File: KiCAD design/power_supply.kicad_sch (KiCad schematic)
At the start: 7 parts, among them U301 A71117CH2-5.0TRG1, U302 MIC5317

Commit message: Fixes
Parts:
- C301: value 10uF -> 1uF; Price 0.29 -> 0.13; PurchaseLoc https://www.digikey.fi/fi/products/detail/yageo/CC0805KKX5R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 -> https://www.digikey.fi/fi/products/detail/yageo/CC0805KKX7R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
- C302: value 22uF -> 1uF; Price 0.09 -> 0.13; PurchaseLoc https://www.digikey.fi/fi/products/detail/yageo/CC0805JRNPO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 -> https://www.digikey.fi/fi/products/detail/yageo/CC0805KKX7R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
- U301: value A71117CH2-5.0TRG1 -> MCP1804T
- U302: PurchaseLoc https://www.digikey.fi/en/products/detail/microchip-technol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 -> https://www.digikey.fi/fi/products/detail/microchip-technol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
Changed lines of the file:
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@@
       (effects (font (size 1.27 1.27)) (justify left))
     )
-    (property "Value" "10uF" (id 1) (at 45.72 62.2362 0)
+    (property "Value" "1uF" (id 1) (at 45.72 62.2362 0)
       (effects (font (size 1.27 1.27)) (justify left))
     )
@@
       (effects (font (size 1.27 1.27)) hide)
     )
-    (property "Datasheet" "https://www.yageo.com/upload/media/product/productsearch/datasheet/mlcc/UPY-GPHC_X5R_4V-to-50V_26.pdf" (id 3) (at 43.18 60.96 0)
+    (property "Datasheet" "https://www.yageo.com/upload/media/product/productsearch/datasheet/mlcc/UPY-GPHC_X7R_6.3V-to-250V_22.pdf" (id 3) (at 43.18 60.96 0)
       (effects (font (size 1.27 1.27)) hide)
     )
-    (property "PurchaseLoc" "https://www.digikey.fi/fi/products/detail/yageo/CC0805KKX5R8BB106/5195275" (id 4) (at 43.18 60.96 0)
+    (property "PurchaseLoc" "https://www.digikey.fi/fi/products/detail/yageo/CC0805KKX7R7BB105/2103103" (id 4) (at 43.18 60.96 0)
       (effects (font (size 1.27 1.27)) hide)
     )
-    (property "Price" "0.29" (id 5) (at 43.18 60.96 0)
+    (property "Price" "0.13" (id 5) (at 43.18 60.96 0)
       (effects (font (size 1.27 1.27)) hide)
     )
@@
       (effects (font (size 1.27 1.27) italic) (justify left) hide)
     )
-    (property "Datasheet" "http://ww1.microchip.com/downloads/en/DeviceDoc/22053C.pdf" (id 3) (at 133.35 59.055 0)
+    (property "Datasheet" "https://ww1.microchip.com/downloads/en/DeviceDoc/MIC5317-High-Performance-Single-150mA-LDO-DS20006195B.pdf" (id 3) (at 133.35 59.055 0)
       (effects (font (size 1.27 1.27)) hide)
     )
-    (property "PurchaseLoc" "https://www.digikey.fi/en/products/detail/microchip-technology/MCP1802T-3302I-OT/1679144" (id 4) (at 133.35 56.515 0)
+    (property "PurchaseLoc" "https://www.digikey.fi/fi/products/detail/microchip-technology/MIC5317-2-8YM5-TR/5049114" (id 4) (at 133.35 56.515 0)
       (effects (font (size 1.27 1.27)) hide)
     )
@@
     (in_bom yes) (on_board yes) (fields_autoplaced)
     (property "Reference" "U301" (id 0) (at 56.134 49.022 0))
-    (property "Value" "A71117CH2-5.0TRG1" (id 1) (at 56.134 51.562 0))
+    (property "Value" "MCP1804T" (id 1) (at 56.134 51.562 0))
     (property "Footprint" "Package_TO_SOT_SMD:SOT-223-3_TabPin2" (id 2) (at 56.134 50.8 0)
       (effects (font (size 1.27 1.27)) hide)
@@
       (effects (font (size 1.27 1.27)) (justify left))
     )
-    (property "Value" "22uF" (id 1) (at 71.12 60.9662 0)
+    (property "Value" "1uF" (id 1) (at 71.12 60.9662 0)
       (effects (font (size 1.27 1.27)) (justify left))
     )
@@
       (effects (font (size 1.27 1.27)) hide)
     )
-    (property "Datasheet" "https://www.yageo.com/upload/media/product/productsearch/datasheet/mlcc/UPY-GP_NP0_16V-to-50V_18.pdf" (id 3) (at 67.818 59.69 0)
+    (property "Datasheet" "https://www.yageo.com/upload/media/product/productsearch/datasheet/mlcc/UPY-GPHC_X7R_6.3V-to-250V_22.pdf" (id 3) (at 67.818 59.69 0)
       (effects (font (size 1.27 1.27)) hide)
     )
-    (property "PurchaseLoc" "https://www.digikey.fi/fi/products/detail/yageo/CC0805JRNPO9BN220/302837" (id 4) (at 67.818 59.69 0)
+    (property "PurchaseLoc" "https://www.digikey.fi/fi/products/detail/yageo/CC0805KKX7R7BB105/2103103" (id 4) (at 67.818 59.69 0)
       (effects (font (size 1.27 1.27)) hide)
     )
-    (property "Price" "0.09" (id 5) (at 67.818 59.69 0)
+    (property "Price" "0.13" (id 5) (at 67.818 59.69 0)
       (effects (font (size 1.27 1.27)) hide)
     )

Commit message: more comments (no changes in functionality)
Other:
- note added: "3.3 V will be used to power the Pmod BLE bluetooth module."
- note added: "5 V voltage will be used to power the TOF sensors, the current sensor, and the Nucleo board."
- note added: "Main power switch."
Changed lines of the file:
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@@
     (stroke (width 0) (type default) (color 0 0 0 0))
+  )
+  (text "Main power switch." (at 182.88 72.39 0)
+    (effects (font (size 1.27 1.27)) (justify left bottom))
   )
   (text "SWITCH" (at 168.275 20.32 0)
@@
     (effects (font (size 3.81 3.81)) (justify left bottom))
   )
+  (text "5 V voltage will be used to power the TOF sensors,\nthe current sensor, and the Nucleo board."
+    (at 16.51 78.74 0)
+    (effects (font (size 1.27 1.27)) (justify left bottom))
+  )
+  (text "3.3 V will be used to power the Pmod BLE bluetooth module."
+    (at 99.06 77.47 0)
+    (effects (font (size 1.27 1.27)) (justify left bottom))
+  )
   (text "Bypass capacitor\nas close to the LDO (pin 1 VIN) as possible\n"

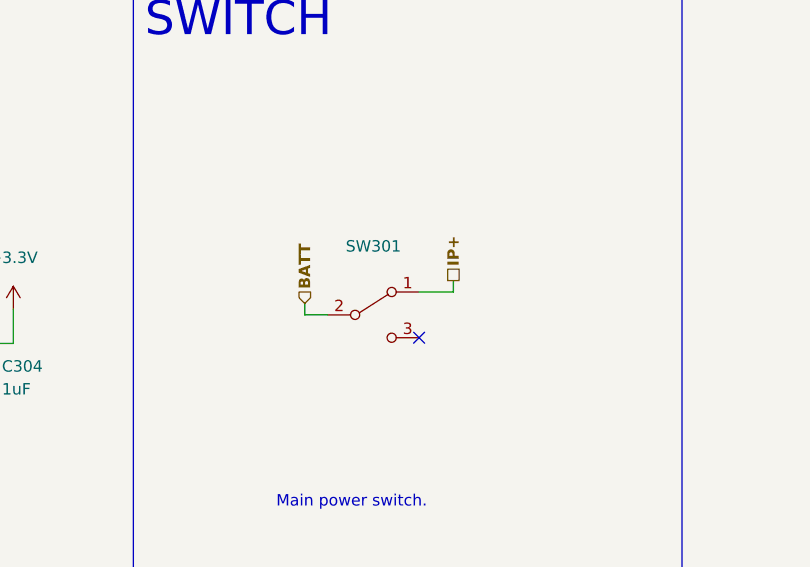
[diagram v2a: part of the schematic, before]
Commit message: change in nucleo pin
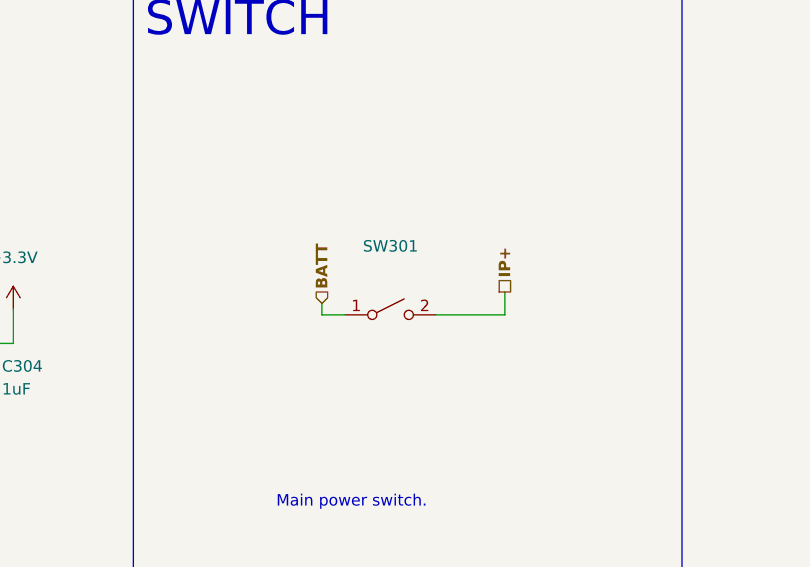
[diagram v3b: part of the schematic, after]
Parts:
- SW301: footprint composants_projet_footprint:1A11-NF5STSE-B -> SWITCH lib:E-SWITCH_RR511D1121; symbol Switch:SW_SPDT -> Switch:SW_SPST
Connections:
- net BATT: now also SW301.1 (A); no longer SW301.2 (B)
- net IP+: now also SW301.2 (B); no longer SW301.1 (A)
- no-connect marks 1 -> 0
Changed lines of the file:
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@@
   (junction (at 120.65 53.975) (diameter 0) (color 0 0 0 0)
   )
-  (no_connect (at 198.755 53.34))
+  (wire (pts (xy 208.28 50.8) (xy 200.66 50.8))
+    (stroke (width 0) (type default) (color 0 0 0 0))
+  )
   (wire (pts (xy 43.18 55.88) (xy 48.514 55.88))
     (stroke (width 0) (type default) (color 0 0 0 0))
@@
     (stroke (width 0) (type default) (color 0 0 0 0))
   )
-  (wire (pts (xy 202.565 48.26) (xy 198.755 48.26))
-    (stroke (width 0) (type default) (color 0 0 0 0))
-  )
   (wire (pts (xy 133.35 65.405) (xy 133.35 66.675))
     (stroke (width 0) (type default) (color 0 0 0 0))
@@
     (stroke (width 0) (type default) (color 0 0 0 0))
   )
-  (wire (pts (xy 188.595 50.8) (xy 186.055 50.8))
+  (wire (pts (xy 190.5 50.8) (xy 187.96 50.8))
     (stroke (width 0) (type default) (color 0 0 0 0))
   )
@@
     (stroke (width 0) (type default) (color 0 0 0 0))
   )
-  (wire (pts (xy 202.565 46.99) (xy 202.565 48.26))
-    (stroke (width 0) (type default) (color 0 0 0 0))
-  )
   (wire (pts (xy 120.65 53.975) (xy 123.19 53.975))
     (stroke (width 0) (type default) (color 0 0 0 0))
@@
     (stroke (width 0) (type default) (color 0 0 0 0))
   )
+  (wire (pts (xy 208.28 48.26) (xy 208.28 50.8))
+    (stroke (width 0) (type default) (color 0 0 0 0))
+  )
   (wire (pts (xy 63.754 55.88) (xy 67.818 55.88))
     (stroke (width 0) (type default) (color 0 0 0 0))
@@
     (stroke (width 0) (type default) (color 0 0 0 0))
   )
-  (wire (pts (xy 186.055 50.8) (xy 186.055 49.53))
+  (wire (pts (xy 187.96 50.8) (xy 187.96 49.53))
     (stroke (width 0) (type default) (color 0 0 0 0))
   )
@@
     (effects (font (size 3.81 3.81)) (justify left bottom))
   )
-  (hierarchical_label "BATT" (shape input) (at 186.055 49.53 90)
+  (hierarchical_label "BATT" (shape input) (at 187.96 49.53 90)
     (effects (font (size 1.27 1.27) bold) (justify left))
   )
-  (hierarchical_label "IP+" (shape passive) (at 202.565 46.99 90)
+  (hierarchical_label "IP+" (shape passive) (at 208.28 48.26 90)
     (effects (font (size 1.27 1.27) bold) (justify left))
   )
@@
     (pin "2")
   )
-  (symbol (lib_id "Switch:SW_SPDT") (at 193.675 50.8 0) (unit 1)
-    (in_bom yes) (on_board yes) (fields_autoplaced)
-    (property "Reference" "SW301" (id 0) (at 193.675 43.18 0))
-    (property "Value" "~" (id 1) (at 193.675 45.72 0))
-    (property "Footprint" "composants_projet_footprint:1A11-NF5STSE-B" (id 2) (at 193.675 50.8 0)
-      (effects (font (size 1.27 1.27)) hide)
-    )
-    (property "Datasheet" "~" (id 3) (at 193.675 50.8 0)
-      (effects (font (size 1.27 1.27)) hide)
-    )
-    (property "Price" "1.05" (id 4) (at 193.675 50.8 0)
-      (effects (font (size 1.27 1.27)) hide)
-    )
-    (property "PurchaseLoc" "https://www.digikey.com/en/products/detail/e-switch/RR511D1121/2116256" (id 5) (at 193.675 50.8 0)
-      (effects (font (size 1.27 1.27)) hide)
-    )
-    (pin "1")
-    (pin "2")
-    (pin "3")
+  (symbol (lib_id "Switch:SW_SPST") (at 195.58 50.8 0) (unit 1)
+    (in_bom yes) (on_board yes) (fields_autoplaced)
+    (property "Reference" "SW301" (id 0) (at 195.58 43.18 0))
+    (property "Value" "~" (id 1) (at 195.58 45.72 0))
+    (property "Footprint" "SWITCH lib:E-SWITCH_RR511D1121" (id 2) (at 195.58 50.8 0)
+      (effects (font (size 1.27 1.27)) hide)
+    )
+    (property "Datasheet" "~" (id 3) (at 195.58 50.8 0)
+      (effects (font (size 1.27 1.27)) hide)
+    )
+    (property "Price" "1.05" (id 4) (at 195.58 50.8 0)
+      (effects (font (size 1.27 1.27)) hide)
+    )
+    (property "PurchaseLoc" "https://www.digikey.com/en/products/detail/e-switch/RR511D1121/2116256" (id 5) (at 195.58 50.8 0)
+      (effects (font (size 1.27 1.27)) hide)
+    )
+    (pin "1")
+    (pin "2")
   )
 )

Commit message: kommentit
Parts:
- U302: Price 0.71 -> 0.21; PurchaseLoc https://www.digikey.fi/fi/products/detail/microchip-technology/MIC5317-2-8YM5-TR/5049114 -> https://www.digikey.fi/fi/products/detail/microchip-technology/MIC5317-3-3YM5-TR/5049120
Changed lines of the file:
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@@
       (effects (font (size 1.27 1.27)) hide)
     )
-    (property "PurchaseLoc" "https://www.digikey.fi/fi/products/detail/microchip-technology/MIC5317-2-8YM5-TR/5049114" (id 4) (at 133.35 56.515 0)
+    (property "PurchaseLoc" "https://www.digikey.fi/fi/products/detail/microchip-technology/MIC5317-3-3YM5-TR/5049120" (id 4) (at 133.35 56.515 0)
       (effects (font (size 1.27 1.27)) hide)
     )
-    (property "Price" "0.71" (id 5) (at 133.35 56.515 0)
+    (property "Price" "0.21" (id 5) (at 133.35 56.515 0)
       (effects (font (size 1.27 1.27)) hide)
     )

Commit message: fixed 3.3 voltage reg
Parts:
- U301: Price 0.94 -> 0.93
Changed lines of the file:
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@@
       (effects (font (size 1.27 1.27)) hide)
     )
-    (property "Price" "0.94" (id 5) (at 56.134 55.88 0)
+    (property "Price" "0.93" (id 5) (at 56.134 55.88 0)
       (effects (font (size 1.27 1.27)) hide)
     )

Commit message: end PCB
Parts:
- U301: Price 0.93 -> 0.94
- U302: Price 0.21 -> 0.71; PurchaseLoc https://www.digikey.fi/fi/products/detail/microchip-technology/MIC5317-3-3YM5-TR/5049120 -> https://www.digikey.fi/fi/products/detail/microchip-technology/MIC5317-2-8YM5-TR/5049114
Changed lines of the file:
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@@
       (effects (font (size 1.27 1.27)) hide)
     )
-    (property "PurchaseLoc" "https://www.digikey.fi/fi/products/detail/microchip-technology/MIC5317-3-3YM5-TR/5049120" (id 4) (at 133.35 56.515 0)
+    (property "PurchaseLoc" "https://www.digikey.fi/fi/products/detail/microchip-technology/MIC5317-2-8YM5-TR/5049114" (id 4) (at 133.35 56.515 0)
       (effects (font (size 1.27 1.27)) hide)
     )
-    (property "Price" "0.21" (id 5) (at 133.35 56.515 0)
+    (property "Price" "0.71" (id 5) (at 133.35 56.515 0)
       (effects (font (size 1.27 1.27)) hide)
     )
@@
       (effects (font (size 1.27 1.27)) hide)
     )
-    (property "Price" "0.93" (id 5) (at 56.134 55.88 0)
+    (property "Price" "0.94" (id 5) (at 56.134 55.88 0)
       (effects (font (size 1.27 1.27)) hide)
     )
